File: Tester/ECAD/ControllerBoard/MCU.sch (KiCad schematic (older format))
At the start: 8 parts, among them U1 ATSAMD21G18A-AUT

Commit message: Progressed circuit design.
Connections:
- net VMCU renamed V3_3
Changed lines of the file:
@@
 	5350 7150 4100 7150
 Text HLabel 1100 900  0    50   Input ~ 0
-VMCU
+V3_3
 Wire Wire Line
 	5550 5700 5350 5700

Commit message: Progressed circuit design.
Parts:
- C15: Manufacturer Part Number (none) -> CC0805MKX7R7BB105
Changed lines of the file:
@@
 F 2 "Capacitor_SMD:C_0805_2012Metric_Pad1.15x1.40mm_HandSolder" H 7288 1550 50  0001 C CNN
 F 3 "~" H 7250 1700 50  0001 C CNN
+F 4 "CC0805MKX7R7BB105" H 7250 1700 50  0001 C CNN "Manufacturer Part Number"
 	1    7250 1700
 	1    0    0    -1

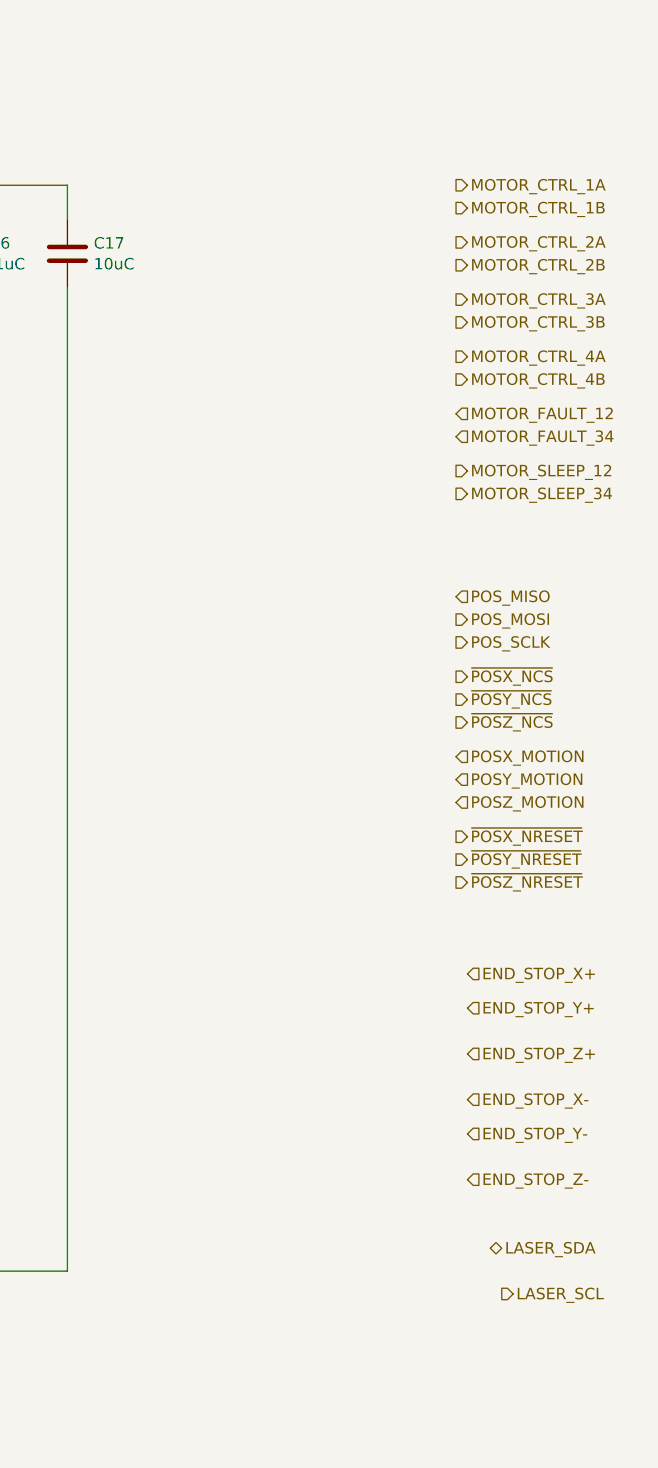
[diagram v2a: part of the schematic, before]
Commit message: Progressed circuit layout.
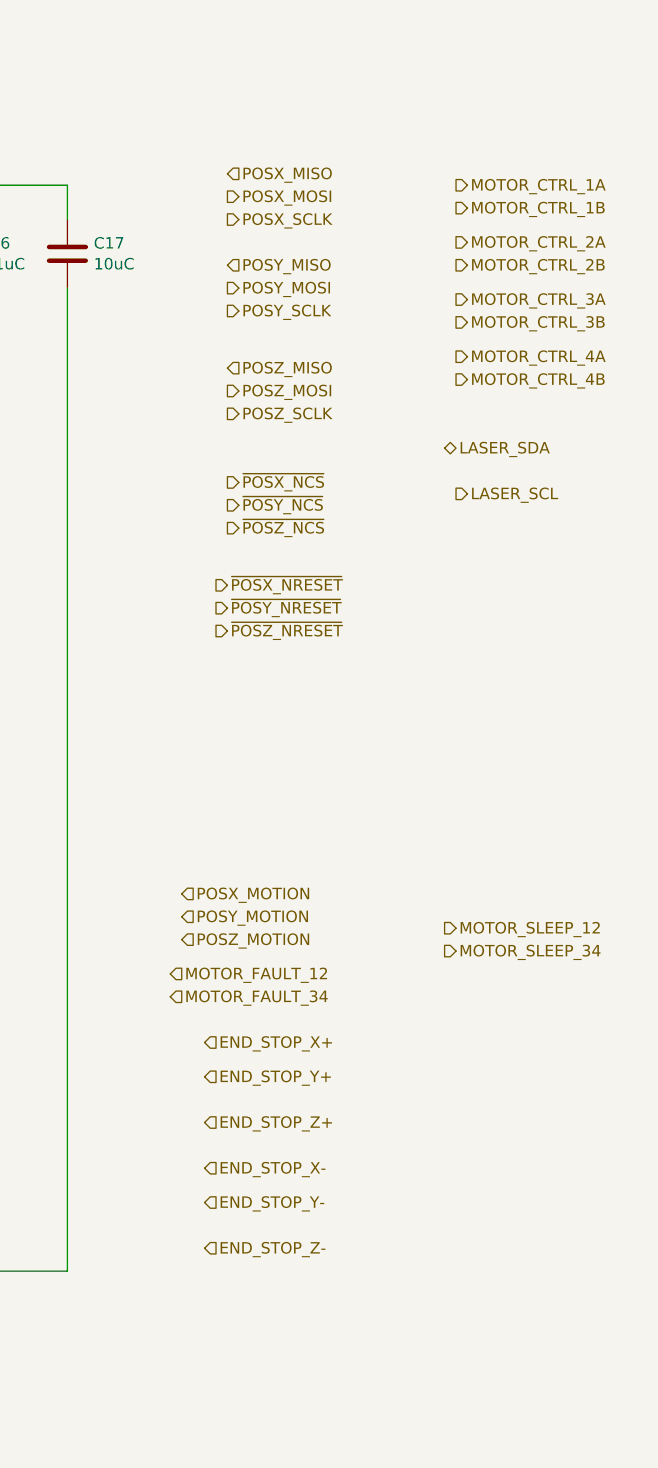
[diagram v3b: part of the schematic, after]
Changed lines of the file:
@@
 $Descr A4 11693 8268
 encoding utf-8
-Sheet 4 5
+Sheet 5 5
 Title ""
 Date ""
@@
 Text HLabel 9900 2250 2    50   Output ~ 0
 MOTOR_CTRL_4B
-Text HLabel 9900 2400 2    50   Input ~ 0
+Text HLabel 8650 4850 2    50   Input ~ 0
 MOTOR_FAULT_12
-Text HLabel 9900 2500 2    50   Input ~ 0
+Text HLabel 8650 4950 2    50   Input ~ 0
 MOTOR_FAULT_34
-Text HLabel 9900 2650 2    50   Output ~ 0
+Text HLabel 9850 4650 2    50   Output ~ 0
 MOTOR_SLEEP_12
-Text HLabel 9900 2750 2    50   Output ~ 0
+Text HLabel 9850 4750 2    50   Output ~ 0
 MOTOR_SLEEP_34
 Text HLabel 1000 7150 0    50   Input ~ 0
@@
 	5550 900  5550 1400
 Connection ~ 5550 1400
-Text HLabel 9900 3200 2    50   Input ~ 0
-POS_MISO
-Text HLabel 9900 3300 2    50   Output ~ 0
-POS_MOSI
-Text HLabel 9900 3400 2    50   Output ~ 0
-POS_SCLK
-Text HLabel 9900 3550 2    50   Output ~ 0
+Text HLabel 8900 1350 2    50   Input ~ 0
+POSX_MISO
+Text HLabel 8900 1450 2    50   Output ~ 0
+POSX_MOSI
+Text HLabel 8900 1550 2    50   Output ~ 0
+POSX_SCLK
+Text HLabel 8900 2700 2    50   Output ~ 0
 ~POSX_NCS
-Text HLabel 9900 3650 2    50   Output ~ 0
+Text HLabel 8900 2800 2    50   Output ~ 0
 ~POSY_NCS
-Text HLabel 9900 3750 2    50   Output ~ 0
+Text HLabel 8900 2900 2    50   Output ~ 0
 ~POSZ_NCS
-Text HLabel 9900 3900 2    50   Input ~ 0
+Text HLabel 8700 4500 2    50   Input ~ 0
 POSX_MOTION
-Text HLabel 9900 4000 2    50   Input ~ 0
+Text HLabel 8700 4600 2    50   Input ~ 0
 POSY_MOTION
-Text HLabel 9900 4100 2    50   Input ~ 0
+Text HLabel 8700 4700 2    50   Input ~ 0
 POSZ_MOTION
-Text HLabel 9900 4250 2    50   Output ~ 0
+Text HLabel 8850 3150 2    50   Output ~ 0
 ~POSX_NRESET
-Text HLabel 9900 4350 2    50   Output ~ 0
+Text HLabel 8850 3250 2    50   Output ~ 0
 ~POSY_NRESET
-Text HLabel 9900 4450 2    50   Output ~ 0
+Text HLabel 8850 3350 2    50   Output ~ 0
 ~POSZ_NRESET
-Text HLabel 9950 4850 2    50   Input ~ 0
+Text HLabel 8800 5150 2    50   Input ~ 0
 END_STOP_X+
-Text HLabel 9950 5000 2    50   Input ~ 0
+Text HLabel 8800 5300 2    50   Input ~ 0
 END_STOP_Y+
-Text HLabel 9950 5200 2    50   Input ~ 0
+Text HLabel 8800 5500 2    50   Input ~ 0
 END_STOP_Z+
-Text HLabel 9950 5400 2    50   Input ~ 0
+Text HLabel 8800 5700 2    50   Input ~ 0
 END_STOP_X-
-Text HLabel 9950 5550 2    50   Input ~ 0
+Text HLabel 8800 5850 2    50   Input ~ 0
 END_STOP_Y-
-Text HLabel 9950 5750 2    50   Input ~ 0
+Text HLabel 8800 6050 2    50   Input ~ 0
 END_STOP_Z-
-Text HLabel 10050 6050 2    50   BiDi ~ 0
+Text HLabel 9850 2550 2    50   BiDi ~ 0
 LASER_SDA
-Text HLabel 10100 6250 2    50   Output ~ 0
+Text HLabel 9900 2750 2    50   Output ~ 0
 LASER_SCL
+Text HLabel 8900 1750 2    50   Input ~ 0
+POSY_MISO
+Text HLabel 8900 1850 2    50   Output ~ 0
+POSY_MOSI
+Text HLabel 8900 1950 2    50   Output ~ 0
+POSY_SCLK
+Text HLabel 8900 2200 2    50   Input ~ 0
+POSZ_MISO
+Text HLabel 8900 2300 2    50   Output ~ 0
+POSZ_MOSI
+Text HLabel 8900 2400 2    50   Output ~ 0
+POSZ_SCLK
 $EndSCHEMATC

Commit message: Progressed circuit layout.
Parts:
- added U?: ATSAMD21J18A-AU, Package_QFP:TQFP-64_10x10mm_P0.5mm, symbol MCU_Microchip_SAMD_Custom:ATSAMD21J18A-AU
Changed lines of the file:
@@
 Text HLabel 8900 2400 2    50   Output ~ 0
 POSZ_SCLK
+$Comp
+L MCU_Microchip_SAMD_Custom:ATSAMD21J18A-AU U?
+U 1 1 5E5C7565
+P 2700 3650
+F 0 "U?" H 2700 1461 50  0000 C CNN
+F 1 "ATSAMD21J18A-AU" H 2700 1370 50  0000 C CNN
+F 2 "Package_QFP:TQFP-64_10x10mm_P0.5mm" H 2250 1000 50  0001 L BNN
+F 3 "" H 2700 3650 50  0001 L BNN
+	1    2700 3650
+	1    0    0    -1
+$EndComp
 $EndSCHEMATC

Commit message: Update MCU.sch
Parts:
- removed U1: ATSAMD21G18A-AUT, Package_QFP:TQFP-48_7x7mm_P0.5mm, symbol MCU_Microchip_SAMD:ATSAMD21G18A-AUT
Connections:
- wire segments 39 -> 34
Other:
- moved on the sheet: C12, C13, C14, C15, C16, C17
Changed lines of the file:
@@
 Comment4 ""
 $EndDescr
-$Comp
-L MCU_Microchip_SAMD:ATSAMD21G18A-AUT U1
-U 1 1 5E507201
-P 5450 3800
-F 0 "U1" H 5450 1811 50  0000 C CNN
-F 1 "ATSAMD21G18A-AUT" H 5450 1720 50  0000 C CNN
-F 2 "Package_QFP:TQFP-48_7x7mm_P0.5mm" H 4500 2050 50  0001 C CNN
-F 3 "http://ww1.microchip.com/downloads/en/DeviceDoc/SAMD21-Family-DataSheet-DS40001882D.pdf" H 5450 4800 50  0001 C CNN
-F 4 "ATSAMD21G18A-AUT" H 5450 3800 50  0001 C CNN "Manufacturer Part Number"
-	1    5450 3800
-	1    0    0    -1
-$EndComp
 Text HLabel 9900 1400 2    50   Output ~ 0
 MOTOR_CTRL_1A
@@
 Text HLabel 1000 7150 0    50   Input ~ 0
 GND
-Wire Wire Line
-	5350 5700 5350 6150
-Wire Wire Line
-	5350 7150 4100 7150
 Text HLabel 1100 900  0    50   Input ~ 0
 V3_3
-Wire Wire Line
-	5550 5700 5350 5700
-Connection ~ 5350 5700
 $Comp
 L Device:C C15
 U 1 1 5E5846F6
-P 7250 1700
-F 0 "C15" H 7365 1746 50  0000 L CNN
-F 1 "1uC" H 7365 1655 50  0000 L CNN
-F 2 "Capacitor_SMD:C_0805_2012Metric_Pad1.15x1.40mm_HandSolder" H 7288 1550 50  0001 C CNN
-F 3 "~" H 7250 1700 50  0001 C CNN
-F 4 "CC0805MKX7R7BB105" H 7250 1700 50  0001 C CNN "Manufacturer Part Number"
-	1    7250 1700
-	1    0    0    -1
-$EndComp
-Wire Wire Line
-	5650 1900 5650 1300
-Wire Wire Line
-	5650 1300 7250 1300
-Wire Wire Line
-	7250 1300 7250 1550
-Wire Wire Line
-	7250 1850 7250 6150
-Wire Wire Line
-	7250 6150 5350 6150
-Connection ~ 5350 6150
-Wire Wire Line
-	5350 6150 5350 7150
+P 6700 1900
+F 0 "C15" H 6815 1946 50  0000 L CNN
+F 1 "1uC" H 6815 1855 50  0000 L CNN
+F 2 "Capacitor_SMD:C_0805_2012Metric_Pad1.15x1.40mm_HandSolder" H 6738 1750 50  0001 C CNN
+F 3 "~" H 6700 1900 50  0001 C CNN
+F 4 "CC0805MKX7R7BB105" H 6700 1900 50  0001 C CNN "Manufacturer Part Number"
+	1    6700 1900
+	1    0    0    -1
+$EndComp
 $Comp
 L Device:C C12
 U 1 1 5E58564D
-P 1700 3600
-F 0 "C12" H 1815 3646 50  0000 L CNN
-F 1 "10uC" H 1815 3555 50  0000 L CNN
-F 2 "Capacitor_SMD:C_0805_2012Metric_Pad1.15x1.40mm_HandSolder" H 1738 3450 50  0001 C CNN
-F 3 "~" H 1700 3600 50  0001 C CNN
-F 4 "CC0805MRX5R6BB106" H 1700 3600 50  0001 C CNN "Manufacturer Part Number"
-	1    1700 3600
-	1    0    0    -1
-$EndComp
-Wire Wire Line
-	1100 900  1700 900
-Wire Wire Line
-	1700 900  1700 3450
-Wire Wire Line
-	1700 3750 1700 7150
-Connection ~ 1700 7150
-Wire Wire Line
-	1700 7150 1000 7150
+P 4650 1900
+F 0 "C12" H 4765 1946 50  0000 L CNN
+F 1 "10uC" H 4765 1855 50  0000 L CNN
+F 2 "Capacitor_SMD:C_0805_2012Metric_Pad1.15x1.40mm_HandSolder" H 4688 1750 50  0001 C CNN
+F 3 "~" H 4650 1900 50  0001 C CNN
+F 4 "CC0805MRX5R6BB106" H 4650 1900 50  0001 C CNN "Manufacturer Part Number"
+	1    4650 1900
+	1    0    0    -1
+$EndComp
 $Comp
 L Device:C C14
 U 1 1 5E586DB7
-P 4100 1700
-F 0 "C14" H 4215 1746 50  0000 L CNN
-F 1 "0.1uC" H 4215 1655 50  0000 L CNN
-F 2 "Capacitor_SMD:C_0805_2012Metric_Pad1.15x1.40mm_HandSolder" H 4138 1550 50  0001 C CNN
-F 3 "~" H 4100 1700 50  0001 C CNN
-F 4 "CC0805ZRY5V8BB104" H 4100 1700 50  0001 C CNN "Manufacturer Part Number"
-	1    4100 1700
-	1    0    0    -1
-$EndComp
-Wire Wire Line
-	5350 1900 5350 1300
-Wire Wire Line
-	5350 1300 4100 1300
-Wire Wire Line
-	4100 1300 4100 1550
-Wire Wire Line
-	4100 1850 4100 7150
-Connection ~ 4100 7150
-Wire Wire Line
-	4100 7150 3550 7150
-Wire Wire Line
-	4100 1300 4100 900
-Wire Wire Line
-	4100 900  3550 900
-Connection ~ 4100 1300
-Connection ~ 1700 900
+P 8200 1900
+F 0 "C14" H 8315 1946 50  0000 L CNN
+F 1 "0.1uC" H 8315 1855 50  0000 L CNN
+F 2 "Capacitor_SMD:C_0805_2012Metric_Pad1.15x1.40mm_HandSolder" H 8238 1750 50  0001 C CNN
+F 3 "~" H 8200 1900 50  0001 C CNN
+F 4 "CC0805ZRY5V8BB104" H 8200 1900 50  0001 C CNN "Manufacturer Part Number"
+	1    8200 1900
+	1    0    0    -1
+$EndComp
 $Comp
 L Device:C C13
 U 1 1 5E588280
-P 3550 1700
-F 0 "C13" H 3665 1746 50  0000 L CNN
-F 1 "0.1uC" H 3665 1655 50  0000 L CNN
-F 2 "Capacitor_SMD:C_0805_2012Metric_Pad1.15x1.40mm_HandSolder" H 3588 1550 50  0001 C CNN
-F 3 "~" H 3550 1700 50  0001 C CNN
-F 4 "CC0805ZRY5V8BB104" H 3550 1700 50  0001 C CNN "Manufacturer Part Number"
-	1    3550 1700
-	1    0    0    -1
-$EndComp
-Wire Wire Line
-	5250 1900 5250 1400
-Wire Wire Line
-	5250 1400 3550 1400
-Wire Wire Line
-	3550 1400 3550 1550
-Wire Wire Line
-	3550 1850 3550 7150
-Connection ~ 3550 7150
-Wire Wire Line
-	3550 7150 1700 7150
-Wire Wire Line
-	3550 1400 3550 900
-Connection ~ 3550 1400
-Connection ~ 3550 900
-Wire Wire Line
-	3550 900  1700 900
-Wire Wire Line
-	5550 1900 5550 1400
-Wire Wire Line
-	5550 1400 7700 1400
-Wire Wire Line
-	7700 1550 7700 1400
-Connection ~ 7700 1400
-Wire Wire Line
-	7700 1850 7700 6150
-Wire Wire Line
-	7700 6150 7250 6150
-Connection ~ 7250 6150
-Connection ~ 7700 6150
+P 8700 1900
+F 0 "C13" H 8815 1946 50  0000 L CNN
+F 1 "0.1uC" H 8815 1855 50  0000 L CNN
+F 2 "Capacitor_SMD:C_0805_2012Metric_Pad1.15x1.40mm_HandSolder" H 8738 1750 50  0001 C CNN
+F 3 "~" H 8700 1900 50  0001 C CNN
+F 4 "CC0805ZRY5V8BB104" H 8700 1900 50  0001 C CNN "Manufacturer Part Number"
+	1    8700 1900
+	1    0    0    -1
+$EndComp
 $Comp
 L Device:C C16
 U 1 1 5E58C2F2
-P 7700 1700
-F 0 "C16" H 7815 1746 50  0000 L CNN
-F 1 "0.1uC" H 7815 1655 50  0000 L CNN
-F 2 "Capacitor_SMD:C_0805_2012Metric_Pad1.15x1.40mm_HandSolder" H 7738 1550 50  0001 C CNN
-F 3 "~" H 7700 1700 50  0001 C CNN
-F 4 "CC0805ZRY5V8BB104" H 7700 1700 50  0001 C CNN "Manufacturer Part Number"
-	1    7700 1700
+P 7200 1900
+F 0 "C16" H 7315 1946 50  0000 L CNN
+F 1 "0.1uC" H 7315 1855 50  0000 L CNN
+F 2 "Capacitor_SMD:C_0805_2012Metric_Pad1.15x1.40mm_HandSolder" H 7238 1750 50  0001 C CNN
+F 3 "~" H 7200 1900 50  0001 C CNN
+F 4 "CC0805ZRY5V8BB104" H 7200 1900 50  0001 C CNN "Manufacturer Part Number"
+	1    7200 1900
 	1    0    0    -1
 $EndComp
@@
 L Device:C C17
 U 1 1 5E58C960
-P 8200 1700
-F 0 "C17" H 8315 1746 50  0000 L CNN
-F 1 "10uC" H 8315 1655 50  0000 L CNN
-F 2 "Capacitor_SMD:C_0805_2012Metric_Pad1.15x1.40mm_HandSolder" H 8238 1550 50  0001 C CNN
-F 3 "~" H 8200 1700 50  0001 C CNN
-F 4 "CC0805MRX5R6BB106" H 8200 1700 50  0001 C CNN "Manufacturer Part Number"
-	1    8200 1700
-	1    0    0    -1
-$EndComp
-Wire Wire Line
-	8200 1550 8200 1400
-Wire Wire Line
-	7700 1400 8200 1400
-Wire Wire Line
-	8200 1850 8200 6150
-Wire Wire Line
-	7700 6150 8200 6150
+P 7700 1900
+F 0 "C17" H 7815 1946 50  0000 L CNN
+F 1 "10uC" H 7815 1855 50  0000 L CNN
+F 2 "Capacitor_SMD:C_0805_2012Metric_Pad1.15x1.40mm_HandSolder" H 7738 1750 50  0001 C CNN
+F 3 "~" H 7700 1900 50  0001 C CNN
+F 4 "CC0805MRX5R6BB106" H 7700 1900 50  0001 C CNN "Manufacturer Part Number"
+	1    7700 1900
+	1    0    0    -1
+$EndComp
 $Comp
 L Device:L L2
@@
 	0    -1   -1   0
 $EndComp
-Wire Wire Line
-	4650 900  4100 900
-Connection ~ 4100 900
-Wire Wire Line
-	4950 900  5550 900
-Wire Wire Line
-	5550 900  5550 1400
-Connection ~ 5550 1400
 Text HLabel 8900 1350 2    50   Input ~ 0
 POSX_MISO
@@
 Text HLabel 9900 2750 2    50   Output ~ 0
 LASER_SCL
-Text HLabel 8900 1750 2    50   Input ~ 0
+Text HLabel 9200 1800 2    50   Input ~ 0
 POSY_MISO
-Text HLabel 8900 1850 2    50   Output ~ 0
+Text HLabel 9200 1900 2    50   Output ~ 0
 POSY_MOSI
-Text HLabel 8900 1950 2    50   Output ~ 0
+Text HLabel 9200 2000 2    50   Output ~ 0
 POSY_SCLK
 Text HLabel 8900 2200 2    50   Input ~ 0
@@
 L MCU_Microchip_SAMD_Custom:ATSAMD21J18A-AU U?
 U 1 1 5E5C7565
-P 2700 3650
-F 0 "U?" H 2700 1461 50  0000 C CNN
-F 1 "ATSAMD21J18A-AU" H 2700 1370 50  0000 C CNN
-F 2 "Package_QFP:TQFP-64_10x10mm_P0.5mm" H 2250 1000 50  0001 L BNN
-F 3 "" H 2700 3650 50  0001 L BNN
-	1    2700 3650
-	1    0    0    -1
-$EndComp
+P 5550 4200
+F 0 "U?" H 5550 2011 50  0000 C CNN
+F 1 "ATSAMD21J18A-AU" H 5550 1920 50  0000 C CNN
+F 2 "Package_QFP:TQFP-64_10x10mm_P0.5mm" H 5100 1550 50  0001 L BNN
+F 3 "" H 5550 4200 50  0001 L BNN
+	1    5550 4200
+	1    0    0    -1
+$EndComp
+Wire Wire Line
+	5300 6300 5400 6300
+Connection ~ 5400 6300
+Wire Wire Line
+	5400 6300 5500 6300
+Connection ~ 5500 6300
+Wire Wire Line
+	5500 6300 5600 6300
+Connection ~ 5600 6300
+Wire Wire Line
+	5600 6300 5750 6300
+Wire Wire Line
+	5300 6300 5100 6300
+Wire Wire Line
+	5100 6300 5100 7150
+Connection ~ 5300 6300
+Wire Wire Line
+	5850 2200 5850 1750
+Wire Wire Line
+	5850 1750 6700 1750
+Wire Wire Line
+	5700 2200 5700 1650
+Wire Wire Line
+	5700 900  4950 900
+Wire Wire Line
+	7200 1750 7200 1650
+Wire Wire Line
+	7200 1650 7700 1650
+Wire Wire Line
+	7700 1650 7700 1750
+Wire Wire Line
+	7200 1650 5700 1650
+Connection ~ 7200 1650
+Connection ~ 5700 1650
+Wire Wire Line
+	5700 1650 5700 900
+Wire Wire Line
+	7700 2050 7450 2050
+Connection ~ 7200 2050
+Wire Wire Line
+	7200 2050 6700 2050
+Wire Wire Line
+	5200 2200 5300 2200
+Connection ~ 5300 2200
+Wire Wire Line
+	5300 2200 5400 2200
+Wire Wire Line
+	5400 2200 5400 1550
+Wire Wire Line
+	5400 1550 8200 1550
+Wire Wire Line
+	8200 1550 8200 1750
+Connection ~ 5400 2200
+Wire Wire Line
+	8200 2050 7700 2050
+Connection ~ 7700 2050
+Wire Wire Line
+	8700 2050 8200 2050
+Connection ~ 8200 2050
+Wire Wire Line
+	8700 1750 8700 1450
+Wire Wire Line
+	8700 1450 5550 1450
+Wire Wire Line
+	5550 1450 5550 2200
+Wire Wire Line
+	5750 6300 7450 6300
+Wire Wire Line
+	7450 6300 7450 2050
+Connection ~ 5750 6300
+Connection ~ 7450 2050
+Wire Wire Line
+	7450 2050 7200 2050
+Connection ~ 6700 2050
+Wire Wire Line
+	4650 1750 4650 900
+Connection ~ 4650 900
+Wire Wire Line
+	4650 2050 6700 2050
+Wire Wire Line
+	1100 900  4650 900
+Wire Wire Line
+	1000 7150 5100 7150
 $EndSCHEMATC

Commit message: Progressed circuit layout.
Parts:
- added J16: Conn_02x05_Odd_Even, symbol Connector_Generic:Conn_02x05_Odd_Even
- gave numbers to parts that had none: 1
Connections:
- wire segments 34 -> 35
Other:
- moved on the sheet: L2
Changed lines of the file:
@@
 L Device:L L2
 U 1 1 5E58F693
-P 4800 900
-F 0 "L2" V 4990 900 50  0000 C CNN
-F 1 "L" V 4899 900 50  0000 C CNN
-F 2 "Inductor_SMD:L_0805_2012Metric_Pad1.15x1.40mm_HandSolder" H 4800 900 50  0001 C CNN
-F 3 "~" H 4800 900 50  0001 C CNN
-F 4 "BLM21SP471SH1D" H 4800 900 50  0001 C CNN "Manufacturer Part Number"
-	1    4800 900
+P 5200 900
+F 0 "L2" V 5390 900 50  0000 C CNN
+F 1 "L" V 5299 900 50  0000 C CNN
+F 2 "Inductor_SMD:L_0805_2012Metric_Pad1.15x1.40mm_HandSolder" H 5200 900 50  0001 C CNN
+F 3 "~" H 5200 900 50  0001 C CNN
+F 4 "BLM21SP471SH1D" H 5200 900 50  0001 C CNN "Manufacturer Part Number"
+	1    5200 900
 	0    -1   -1   0
 $EndComp
@@
 POSZ_SCLK
 $Comp
-L MCU_Microchip_SAMD_Custom:ATSAMD21J18A-AU U?
+L MCU_Microchip_SAMD_Custom:ATSAMD21J18A-AU U1
 U 1 1 5E5C7565
 P 5550 4200
-F 0 "U?" H 5550 2011 50  0000 C CNN
+F 0 "U1" H 5550 2011 50  0000 C CNN
 F 1 "ATSAMD21J18A-AU" H 5550 1920 50  0000 C CNN
 F 2 "Package_QFP:TQFP-64_10x10mm_P0.5mm" H 5100 1550 50  0001 L BNN
@@
 	5700 2200 5700 1650
 Wire Wire Line
-	5700 900  4950 900
+	5700 900  5350 900
 Wire Wire Line
 	7200 1750 7200 1650
@@
 Wire Wire Line
 	1000 7150 5100 7150
+Wire Wire Line
+	4650 900  5050 900
+$Comp
+L Connector_Generic:Conn_02x05_Odd_Even J16
+U 1 1 5E5DF00C
+P 2600 2150
+F 0 "J16" H 2650 2567 50  0000 C CNN
+F 1 "Conn_02x05_Odd_Even" H 2650 2476 50  0000 C CNN
+F 2 "" H 2600 2150 50  0001 C CNN
+F 3 "~" H 2600 2150 50  0001 C CNN
+	1    2600 2150
+	1    0    0    -1
+$EndComp
 $EndSCHEMATC
